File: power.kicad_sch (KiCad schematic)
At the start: 18 parts, among them U4 SPX3819M5-L-3-3, U7 LMR14020SDDAR

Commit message: Update placement
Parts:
- C17, C23: footprint Capacitor_SMD:C_0603_1608Metric -> Capacitor_SMD:C_0402_1005Metric
- C24: value 0.1u -> 100n; footprint Capacitor_SMD:C_0603_1608Metric -> Capacitor_SMD:C_0402_1005Metric

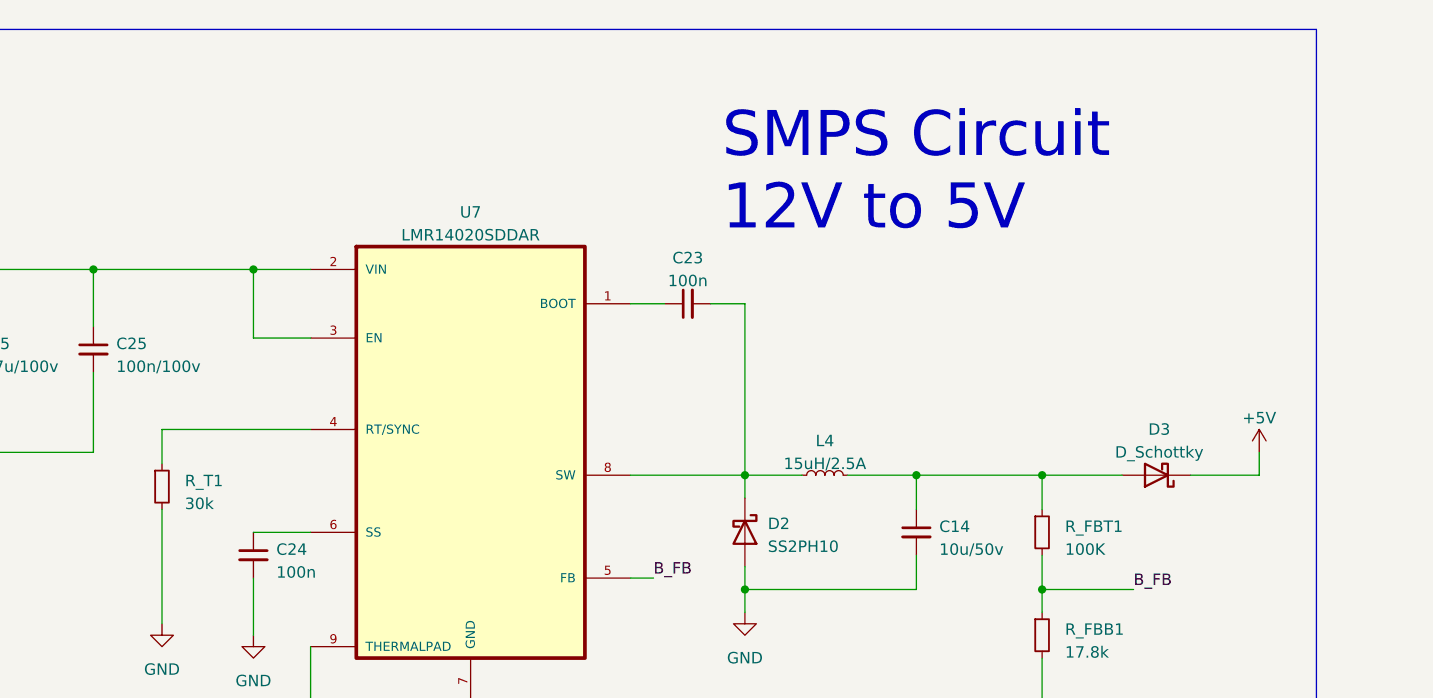
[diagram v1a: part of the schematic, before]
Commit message: route usb and flash
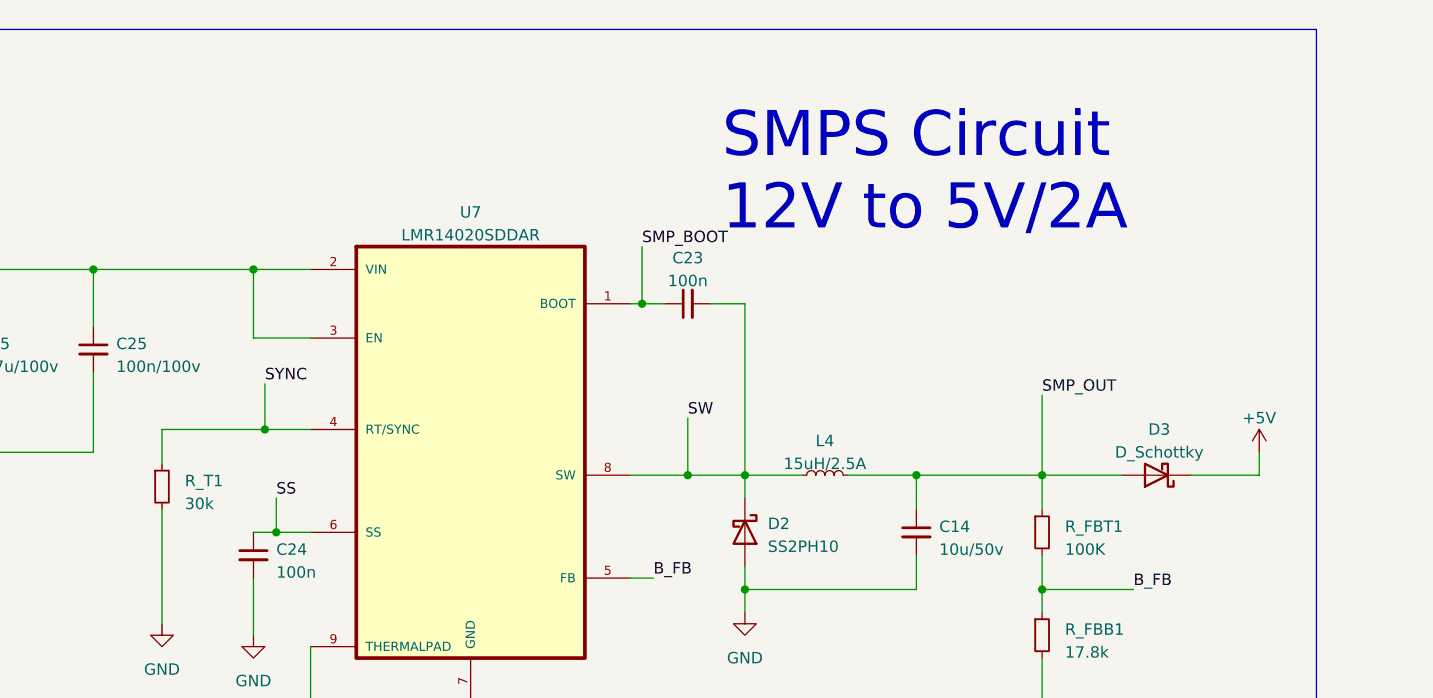
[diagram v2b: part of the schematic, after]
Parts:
- C14: LCSC (none) -> C72487
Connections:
- net SS: now reaches C24.1, U7.6 (SS)
- net SMP_OUT: now reaches C14.1, D3.2 (A), L4.2, R_FBT1.1
- net SMP_BOOT: now reaches C23.1, U7.1 (BOOT)
- net SW: now reaches C23.2, D2.1 (K), L4.1, U7.8 (SW)
- net SYNC: now reaches R_T1.1, U7.4 (RT/SYNC)
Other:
- note added: "SMPS Circuit 12V to 5V/2A"
- note removed: "SMPS Circuit 12V to 5V"
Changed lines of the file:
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@@
   (junction (at 38.1 113.03) (diameter 0) (color 0 0 0 0)
   )
+  (junction (at 119.38 135.89) (diameter 0) (color 0 0 0 0)
+  )
+  (junction (at 114.3 116.84) (diameter 0) (color 0 0 0 0)
+  )
+  (junction (at 73.66 142.24) (diameter 0) (color 0 0 0 0)
+  )
   (junction (at 53.34 113.03) (diameter 0) (color 0 0 0 0)
   )
@@
   (junction (at 71.12 113.03) (diameter 0) (color 0 0 0 0)
   )
+  (junction (at 72.39 130.81) (diameter 0) (color 0 0 0 0)
+  )
   (junction (at 95.25 163.83) (diameter 0) (color 0 0 0 0)
   )
@@
     (stroke (width 0) (type default))
   )
+  (wire (pts (xy 114.3 110.49) (xy 114.3 116.84))
+    (stroke (width 0) (type default))
+  )
   (wire (pts (xy 38.1 124.46) (xy 38.1 133.35))
     (stroke (width 0) (type default))
   )
+  (wire (pts (xy 158.75 127) (xy 158.75 135.89))
+    (stroke (width 0) (type default))
+  )
   (wire (pts (xy 306.07 147.32) (xy 306.07 158.75))
     (stroke (width 0) (type default))
@@
     (stroke (width 0) (type default))
   )
-  (wire (pts (xy 77.47 130.81) (xy 60.96 130.81))
+  (wire (pts (xy 77.47 130.81) (xy 72.39 130.81))
     (stroke (width 0) (type default))
   )
@@
     (stroke (width 0) (type default))
   )
+  (wire (pts (xy 72.39 130.81) (xy 60.96 130.81))
+    (stroke (width 0) (type default))
+  )
   (wire (pts (xy 306.07 162.56) (xy 318.77 162.56))
     (stroke (width 0) (type default))
@@
     (stroke (width 0) (type default))
   )
+  (wire (pts (xy 119.38 129.54) (xy 119.38 135.89))
+    (stroke (width 0) (type default))
+  )
   (wire (pts (xy 283.21 158.75) (xy 306.07 158.75))
     (stroke (width 0) (type default))
   )
+  (wire (pts (xy 73.66 142.24) (xy 77.47 142.24))
+    (stroke (width 0) (type default))
+  )
   (wire (pts (xy 38.1 106.68) (xy 38.1 113.03))
     (stroke (width 0) (type default))
@@
     (stroke (width 0) (type default))
   )
+  (wire (pts (xy 119.38 135.89) (xy 125.73 135.89))
+    (stroke (width 0) (type default))
+  )
   (wire (pts (xy 158.75 144.78) (xy 158.75 148.59))
     (stroke (width 0) (type default))
@@
     (stroke (width 0) (type default))
   )
+  (wire (pts (xy 114.3 116.84) (xy 116.84 116.84))
+    (stroke (width 0) (type default))
+  )
   (wire (pts (xy 53.34 124.46) (xy 53.34 133.35))
     (stroke (width 0) (type default))
@@
     (stroke (width 0) (type default))
   )
+  (wire (pts (xy 73.66 138.43) (xy 73.66 142.24))
+    (stroke (width 0) (type default))
+  )
   (wire (pts (xy 328.93 152.4) (xy 328.93 162.56))
     (stroke (width 0) (type default))
@@
     (stroke (width 0) (type default))
   )
-  (wire (pts (xy 113.03 116.84) (xy 116.84 116.84))
+  (wire (pts (xy 113.03 116.84) (xy 114.3 116.84))
     (stroke (width 0) (type default))
   )
@@
     (stroke (width 0) (type default))
   )
-  (wire (pts (xy 113.03 135.89) (xy 125.73 135.89))
+  (wire (pts (xy 113.03 135.89) (xy 119.38 135.89))
     (stroke (width 0) (type default))
   )
@@
     (stroke (width 0) (type default))
   )
-  (wire (pts (xy 71.12 142.24) (xy 77.47 142.24))
+  (wire (pts (xy 71.12 142.24) (xy 73.66 142.24))
     (stroke (width 0) (type default))
   )
@@
     (stroke (width 0) (type default))
   )
+  (wire (pts (xy 72.39 125.73) (xy 72.39 130.81))
+    (stroke (width 0) (type default))
+  )
   (wire (pts (xy 71.12 147.32) (xy 71.12 153.67))
     (stroke (width 0) (type default))
@@
     (fill (type none))
   )
-  (text "SMPS Circuit\n12V to 5V\n" (at 123.19 109.22 0)
+  (text "SMPS Circuit\n12V to 5V/2A\n" (at 123.19 109.22 0)
     (effects (font (size 5 5)) (justify left bottom))
   )
@@
     (effects (font (size 4.5 4.5)) (justify left bottom))
   )
+  (label "SYNC" (at 72.39 125.73 0) (fields_autoplaced)
+    (effects (font (size 1.27 1.27)) (justify left bottom))
+  )
+  (label "SMP_BOOT" (at 114.3 110.49 0) (fields_autoplaced)
+    (effects (font (size 1.27 1.27)) (justify left bottom))
+  )
   (label "B_FB" (at 115.57 147.32 0) (fields_autoplaced)
     (effects (font (size 1.27 1.27)) (justify left bottom))
   )
+  (label "SS" (at 73.66 138.43 0) (fields_autoplaced)
+    (effects (font (size 1.27 1.27)) (justify left bottom))
+  )
+  (label "SMP_OUT" (at 158.75 127 0) (fields_autoplaced)
+    (effects (font (size 1.27 1.27)) (justify left bottom))
+  )
   (label "B_FB" (at 168.91 148.59 0) (fields_autoplaced)
+    (effects (font (size 1.27 1.27)) (justify left bottom))
+  )
+  (label "SW" (at 119.38 129.54 0) (fields_autoplaced)
     (effects (font (size 1.27 1.27)) (justify left bottom))
   )
@@
   )
   (symbol (lib_id "Device:C_Small") (at 144.78 142.24 0) (unit 1)
-    (in_bom yes) (on_board yes) (dnp no) (fields_autoplaced)
+    (in_bom yes) (on_board yes) (dnp no)
     (property "Reference" "C14" (at 147.32 141.6113 0)
       (effects (font (size 1.27 1.27)) (justify left))
@@
       (effects (font (size 1.27 1.27)) (justify left))
     )
-    (property "Footprint" "Capacitor_SMD:C_1210_3225Metric" (at 144.78 142.24 0)
+    (property "Footprint" "Capacitor_SMD:C_1210_3225Metric" (at 144.78 152.4 0)
       (effects (font (size 1.27 1.27)) hide)
     )
@@
       (effects (font (size 1.27 1.27)) hide)
     )
+    (property "LCSC" "C72487" (at 144.78 142.24 0)
+      (effects (font (size 1.27 1.27)) hide)
+    )

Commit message: route motors
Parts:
- renumbered C15 to C1, C25 to C2, C24 to C3, C23 to C4, C14 to C5, C16 to C6, C17 to C7, C18 to C8, D2 to D1, D3 to D2, D1 to D3, L4 to L1, R7 to R1, U7 to U1, U4 to U2

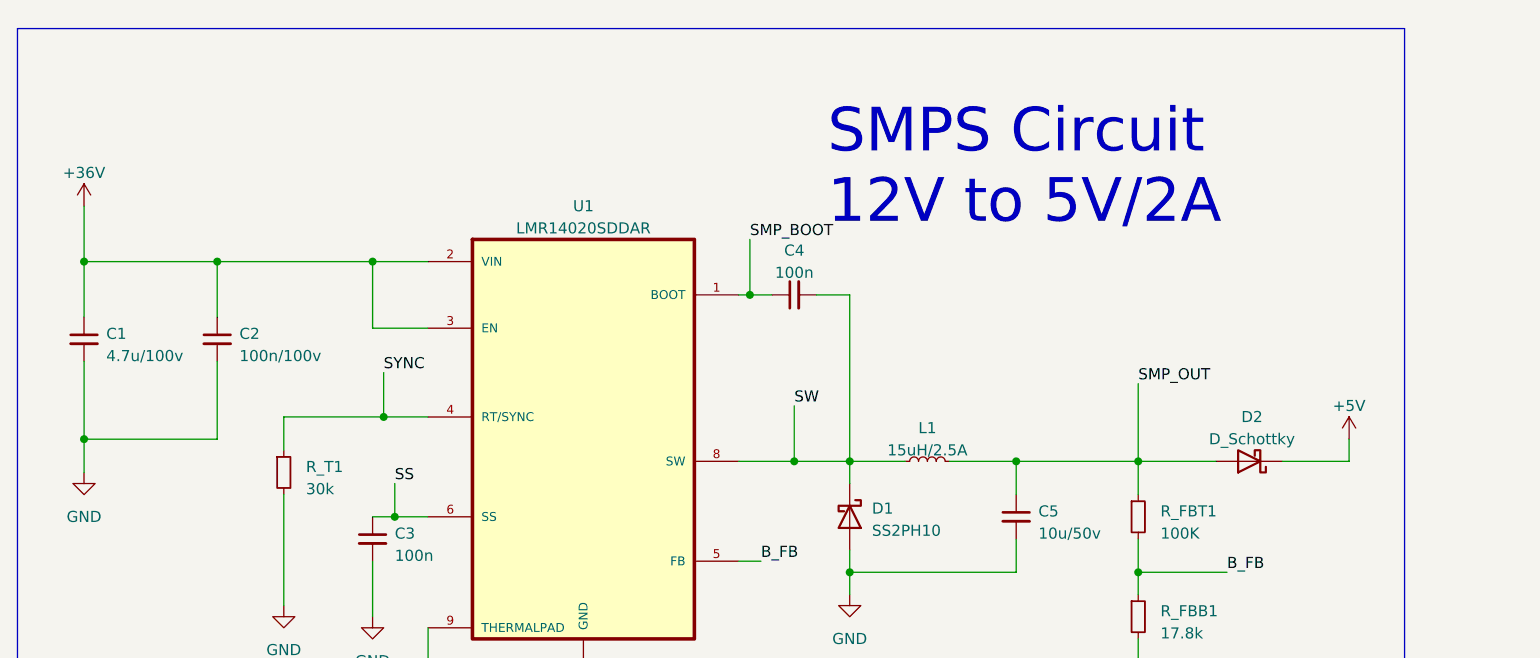
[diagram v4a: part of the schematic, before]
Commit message: Update capacitor footprints
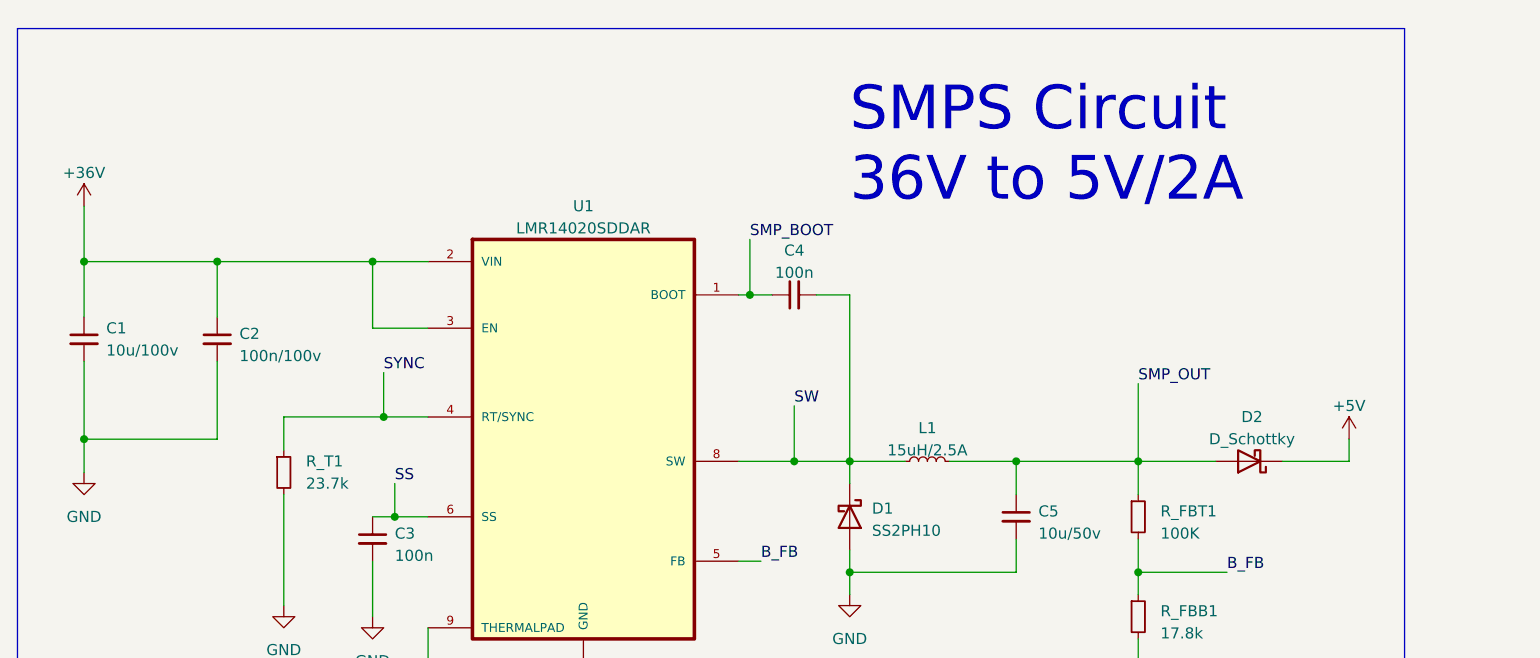
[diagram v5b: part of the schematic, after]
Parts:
- C1: value 4.7u/100v -> 10u/100v; footprint Capacitor_SMD:C_1812_4532Metric -> Capacitor_SMD:C_1210_3225Metric; LCSC (none) -> C5156756
- C2: footprint Capacitor_SMD:C_0805_2012Metric -> Capacitor_SMD:C_0603_1608Metric; LCSC (none) -> C88219
- R_T1: value 30k -> 23.7k
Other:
- note added: "SMPS Circuit 36V to 5V/2A"
- note removed: "SMPS Circuit 12V to 5V/2A"
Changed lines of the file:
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@@
     (fill (type none))
   )
-  (text "SMPS Circuit\n12V to 5V/2A\n" (at 123.19 109.22 0)
+  (text "SMPS Circuit\n36V to 5V/2A\n" (at 125.73 106.68 0)
     (effects (font (size 5 5)) (justify left bottom))
   )
@@
       (effects (font (size 1.27 1.27)) (justify left))
     )
-    (property "Footprint" "Capacitor_SMD:C_0805_2012Metric" (at 53.34 121.92 0)
+    (property "Footprint" "Capacitor_SMD:C_0603_1608Metric" (at 53.34 121.92 0)
       (effects (font (size 1.27 1.27)) hide)
     )
@@
       (effects (font (size 1.27 1.27)) hide)
     )
+    (property "LCSC" "C88219" (at 53.34 121.92 0)
+      (effects (font (size 1.27 1.27)) hide)
+    )
     (pin "1")
     (pin "2")
@@
   (symbol (lib_id "Device:C_Small") (at 38.1 121.92 0) (unit 1)
     (in_bom yes) (on_board yes) (dnp no) (fields_autoplaced)
-    (property "Reference" "C1" (at 40.64 121.2913 0)
-      (effects (font (size 1.27 1.27)) (justify left))
-    )
-    (property "Value" "4.7u/100v" (at 40.64 123.8313 0)
-      (effects (font (size 1.27 1.27)) (justify left))
-    )
-    (property "Footprint" "Capacitor_SMD:C_1812_4532Metric" (at 38.1 121.92 0)
+    (property "Reference" "C1" (at 40.64 120.6563 0)
+      (effects (font (size 1.27 1.27)) (justify left))
+    )
+    (property "Value" "10u/100v" (at 40.64 123.1963 0)
+      (effects (font (size 1.27 1.27)) (justify left))
+    )
+    (property "Footprint" "Capacitor_SMD:C_1210_3225Metric" (at 38.1 121.92 0)
       (effects (font (size 1.27 1.27)) hide)
     )
     (property "Datasheet" "~" (at 38.1 121.92 0)
+      (effects (font (size 1.27 1.27)) hide)
+    )
+    (property "LCSC" "C5156756" (at 38.1 121.92 0)
       (effects (font (size 1.27 1.27)) hide)
     )
@@
   (symbol (lib_id "Device:R_Small") (at 60.96 137.16 0) (unit 1)
     (in_bom yes) (on_board yes) (dnp no) (fields_autoplaced)
-    (property "Reference" "R_T1" (at 63.5 136.525 0)
-      (effects (font (size 1.27 1.27)) (justify left))
-    )
-    (property "Value" "30k" (at 63.5 139.065 0)
-      (effects (font (size 1.27 1.27)) (justify left))
-    )
+    (property "Reference" "R_T1" (at 63.5 135.89 0)
+      (effects (font (size 1.27 1.27)) (justify left))
+    )
+    (property "Value" "23.7k" (at 63.5 138.43 0)
+      (effects (font (size 1.27 1.27)) (justify left))
+    )

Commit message: pcb updates & improvements
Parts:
- D2: value D_Schottky -> SS2PH10
- R1: value 1k -> 330R
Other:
- moved on the sheet: C1, C2, C3, C4, C5, C6, C7, C8, D1, D2, D3, L1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
